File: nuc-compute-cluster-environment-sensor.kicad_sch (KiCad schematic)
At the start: 98 parts

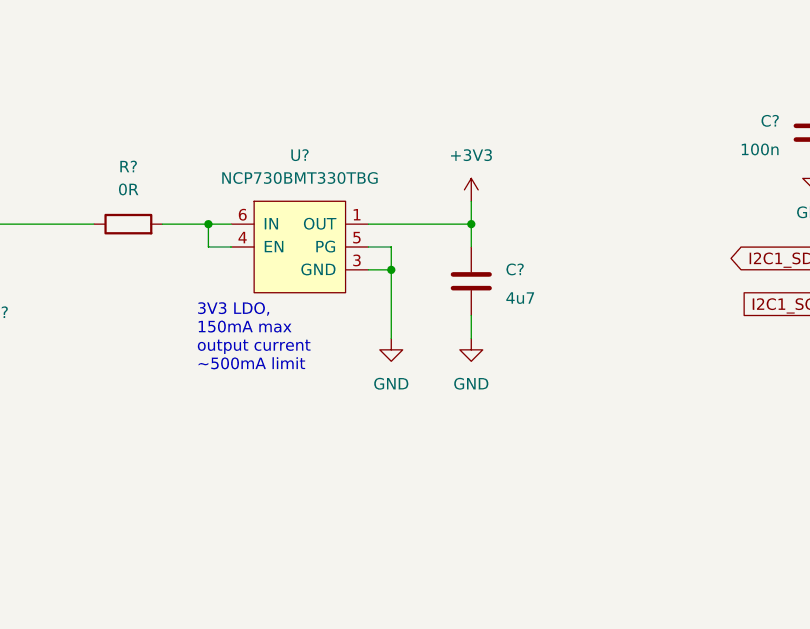
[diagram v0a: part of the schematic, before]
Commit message: [#39832] SCH: Add 3V3 LDO Power Good testpoint, update remarks
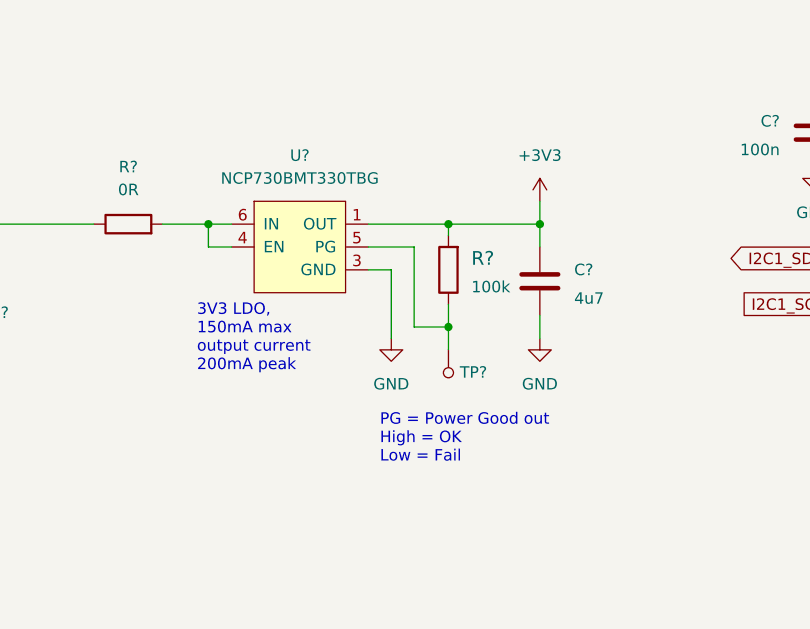
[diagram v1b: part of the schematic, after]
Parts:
- added R?: R_100k_0402, antmicro-footprints:0402-res, symbol antmicroResistors0402:R_100k_0402
- added TP?: TP_SMD1MM, antmicro-footprints:Testpoint_smd_1mm, symbol antmicroTestPoints:TP_SMD1MM
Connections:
- net +3V3: now also R?.2
- net GND: no longer U?.5 (PG)
- new net: R?.1, TP?.1, U?.5 (PG)
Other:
- note added: "3V3 LDO, 150mA max output current 200mA peak"
- note added: "PG = Power Good out High = OK Low = Fail"
- note removed: "3V3 LDO, 150mA max output current ~500mA limit"
- moved on the sheet: C?

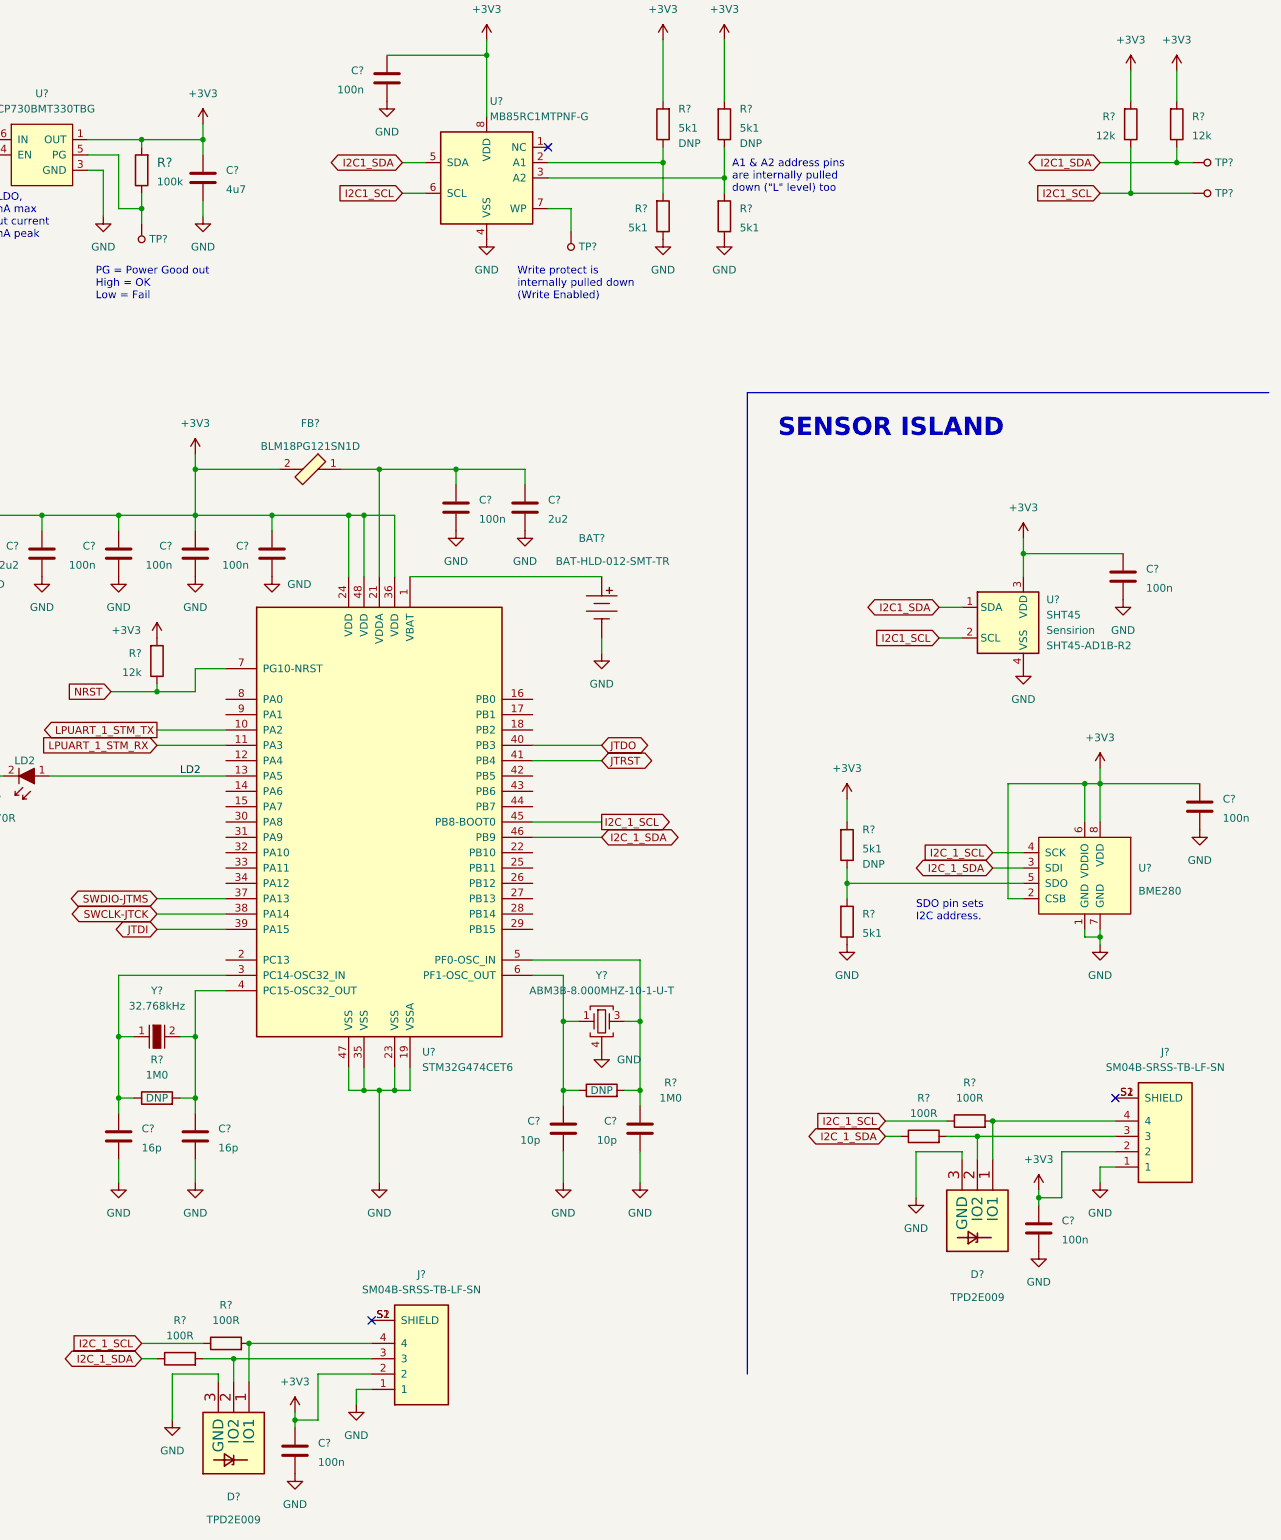
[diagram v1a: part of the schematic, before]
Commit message: [#39832] SCH: Add ESD protection diodes for 3V3 pins in QWIIC connectors, change most pull-ups to 100k
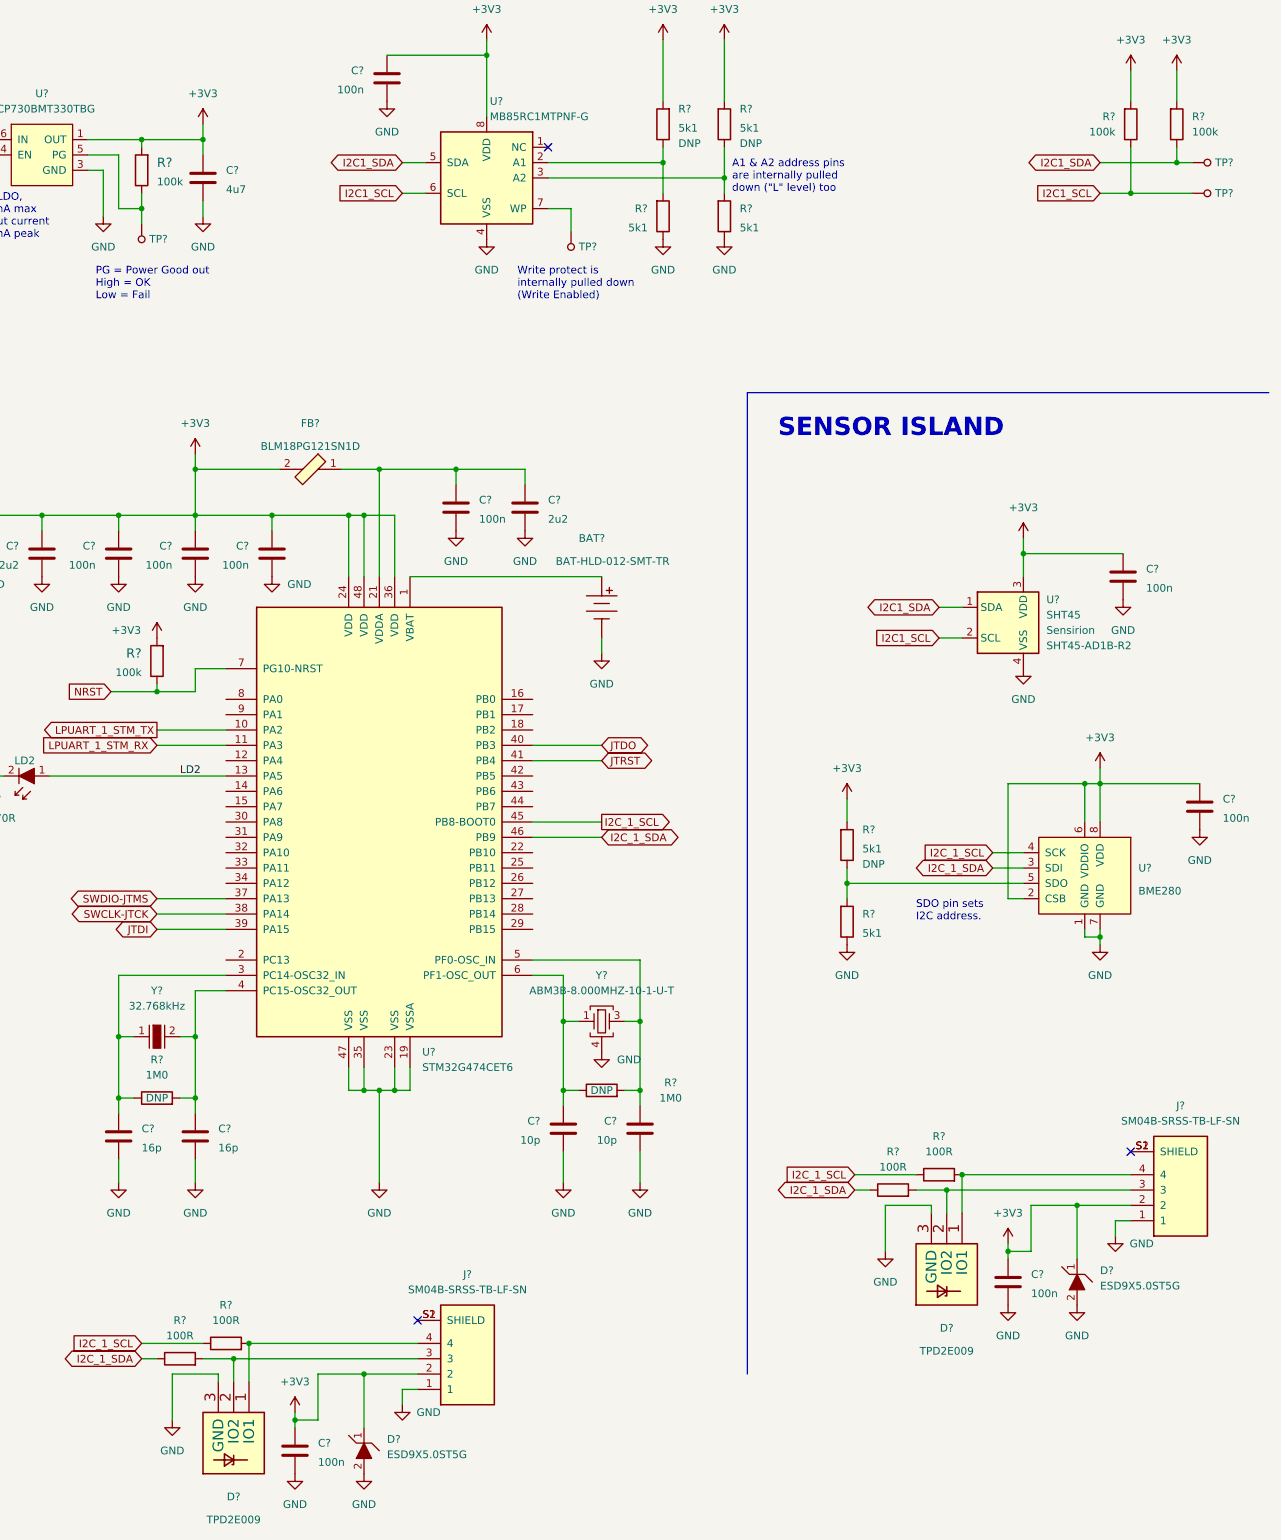
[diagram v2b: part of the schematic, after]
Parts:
- removed C?: C_100n_0402, antmicro-footprints:0402-cap, symbol antmicroCapacitors0402:C_100n_0402
- removed D?: TPD2E009, antmicro-footprints:SOT-723, symbol antmicroTVSDiodes:TPD2E009
- removed J?: SM04B-SRSS-TB-LF-SN, antmicro-footprints:SM04B-SRSS-TB-LF-SN, symbol antmicroRectangularConnectorsHeadersMalePins:SM04B-SRSS-TB-LF-SN
- removed R? (x2): R_100R_0402, antmicro-footprints:0402-res, symbol antmicroResistors0402:R_100R_0402
- removed R?: R_12k_0402, antmicro-footprints:0402-res, symbol antmicroResistors0402:R_12k_0402
- added C?: C_100n_0402, antmicro-footprints:0402-cap, symbol antmicroCapacitors0402:C_100n_0402
- added D? (x2): ESD9X5.0ST5G, antmicro-footprints:SOD-923, symbol antmicroTVSDiodes:ESD9X5.0ST5G
- added D?: TPD2E009, antmicro-footprints:SOT-723, symbol antmicroTVSDiodes:TPD2E009
- added J?: SM04B-SRSS-TB-LF-SN, antmicro-footprints:SM04B-SRSS-TB-LF-SN, symbol antmicroRectangularConnectorsHeadersMalePins:SM04B-SRSS-TB-LF-SN
- added R? (x2): R_100R_0402, antmicro-footprints:0402-res, symbol antmicroResistors0402:R_100R_0402
- added R?: R_100k_0402, antmicro-footprints:0402-res, symbol antmicroResistors0402:R_100k_0402
- R? (x2): value R_12k_0402 -> R_100k_0402; symbol antmicroResistors0402:R_12k_0402 -> antmicroResistors0402:R_100k_0402; MPN CRCW040212K0FKEDHP -> CRCW0402100KFKEDHP; Val 12k -> 100k
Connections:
- net +3V3: now also C?.2, D?.1, D?.1, J?.2, R?.2
- net GND: now also C?.1, D?.2, D?.2, D?.3 (GND), J?.1
- net I2C_1_SCL: now also R?.1
- net I2C_1_SDA: now also R?.1
- net NRST: now also R?.1
- new net: D?.2 (IO2), J?.3, R?.2
- new net: D?.1 (IO1), J?.4, R?.2
- new net: J?.S1 (SHIELD), J?.S2 (SHIELD)
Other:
- moved on the sheet: J?

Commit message: [#39832] SCH: Divide schematic into sections, add section titles
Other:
- note added: "3V3 Regulator"
- note added: "FTDI USB-UART/I2C/JTAG Bridge"
- note added: "Fujitsu FeRAM I2C Memory"
- note added: "I2C pull-ups & Test-Points"
- note added: "Island Qwiic connector"
- note added: "Mainland Qwiic connector"
- note added: "STM32 Main Microcontroller"
- note added: "USB-C 2.0 Data & Power connector"

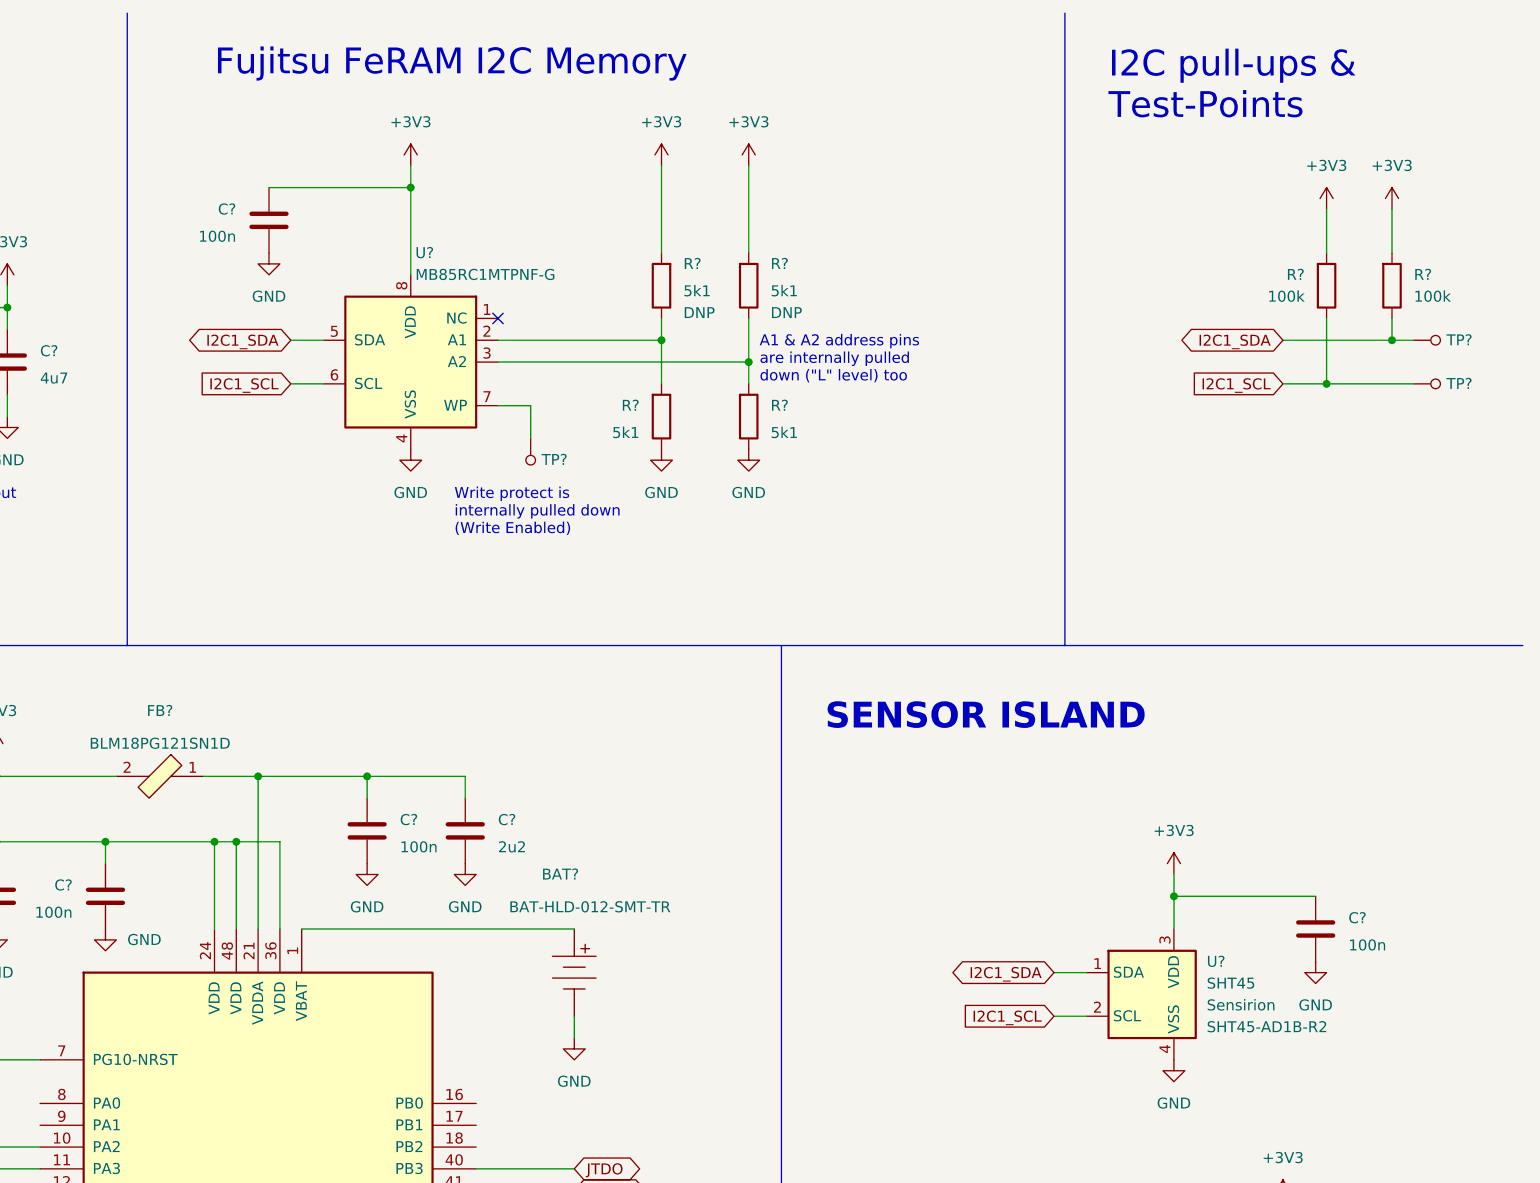
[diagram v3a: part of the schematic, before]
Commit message: [#39832] SCH: Fix typos in I2C labels
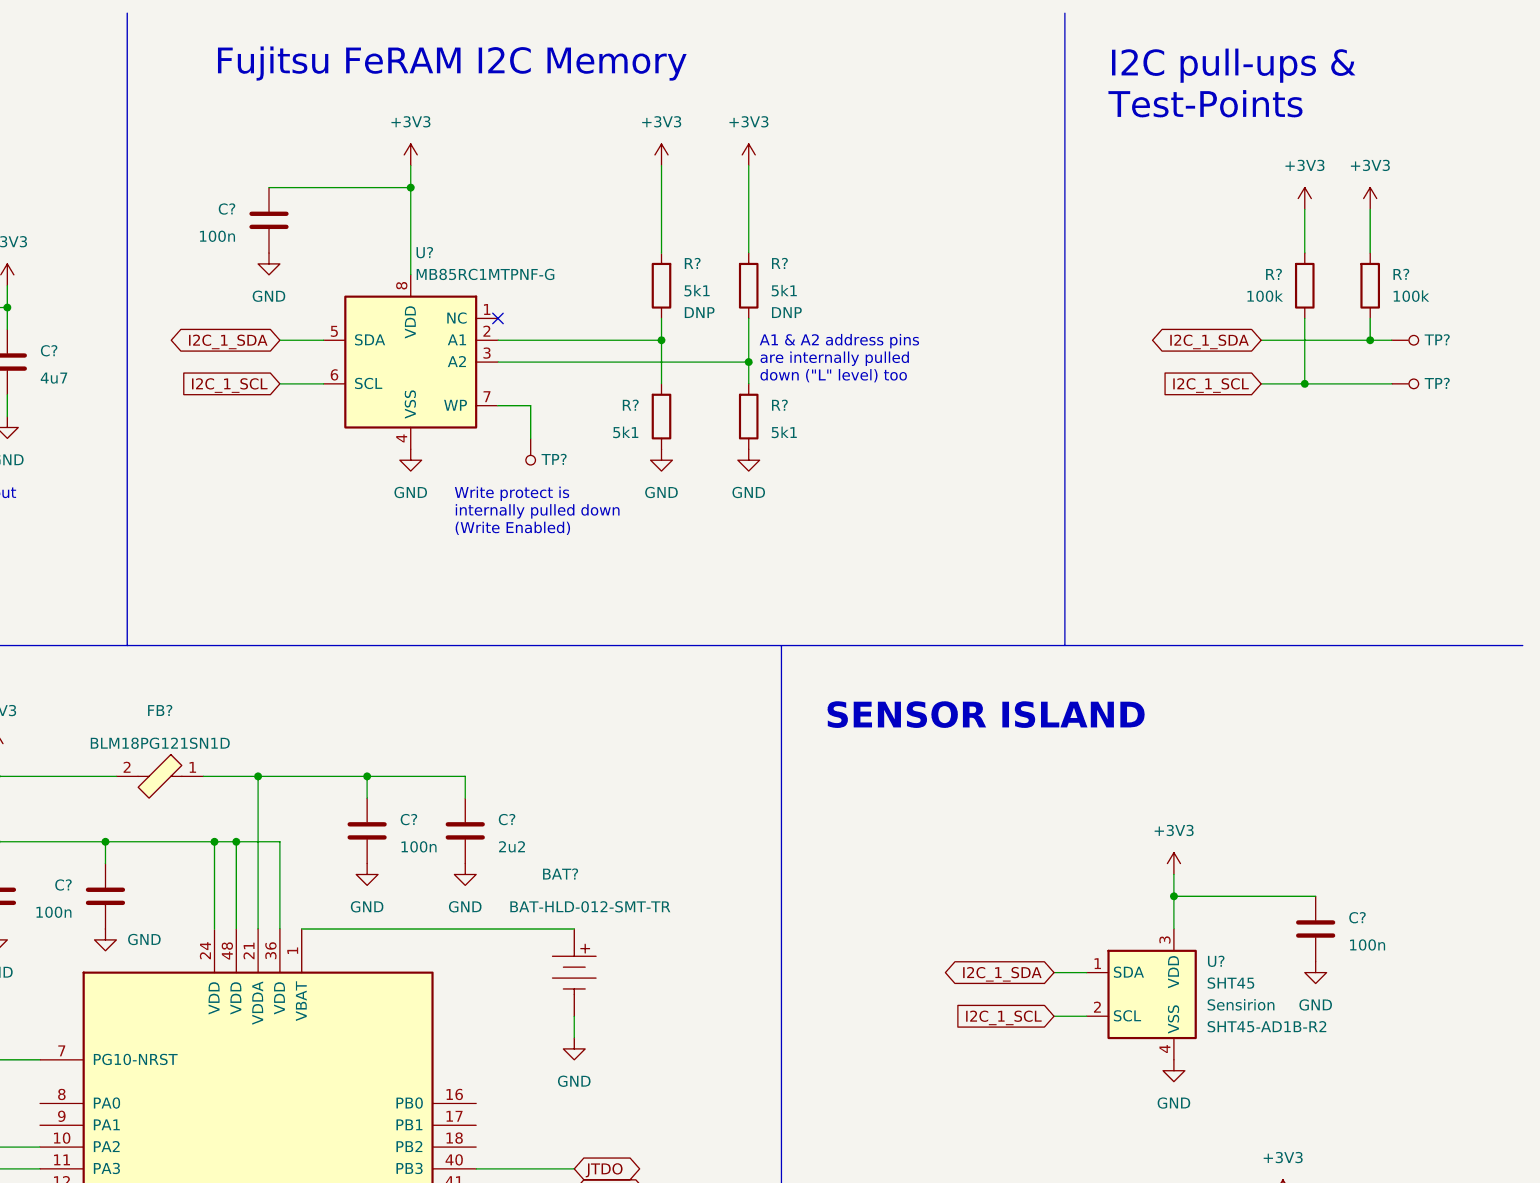
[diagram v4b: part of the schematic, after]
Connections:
- net I2C1_SCL is gone; now on net I2C_1_SCL: R?.1, TP?.1, U?.2 (SCL), U?.6 (SCL)
- net I2C1_SDA is gone; now on net I2C_1_SDA: R?.1, TP?.1, U?.1 (SDA), U?.5 (SDA)
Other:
- moved on the sheet: R?, TP?

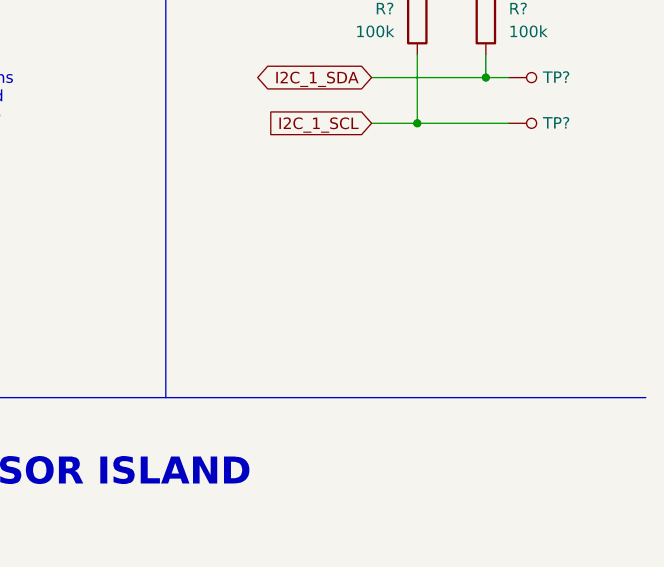
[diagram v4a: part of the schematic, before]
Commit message: [#39832] SCH: Add extra 3V3 and GND test-points
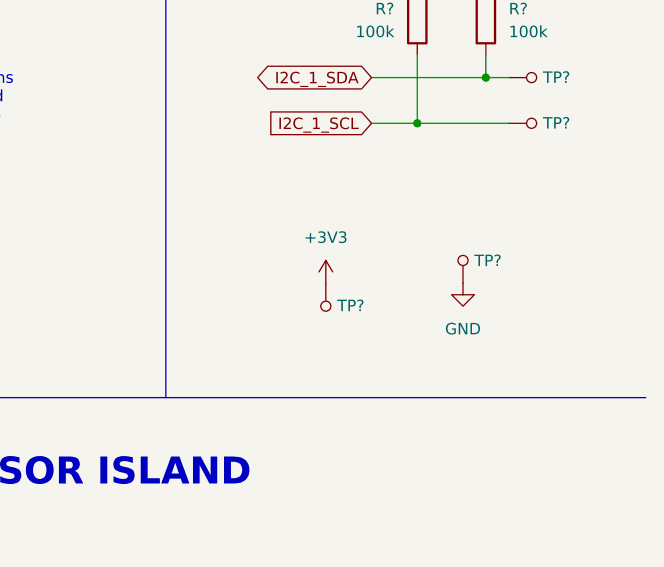
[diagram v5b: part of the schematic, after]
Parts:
- added TP? (x2): TP_SMD1MM, antmicro-footprints:Testpoint_smd_1mm, symbol antmicroTestPoints:TP_SMD1MM
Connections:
- net +3V3: now also TP?.1
- net GND: now also TP?.1
